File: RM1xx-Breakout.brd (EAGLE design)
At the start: 66.7 x 36.8 mm, 27 parts, among them IC3 MCP1703, J1 JUMPER_1X30805, J6 Lipo Battery

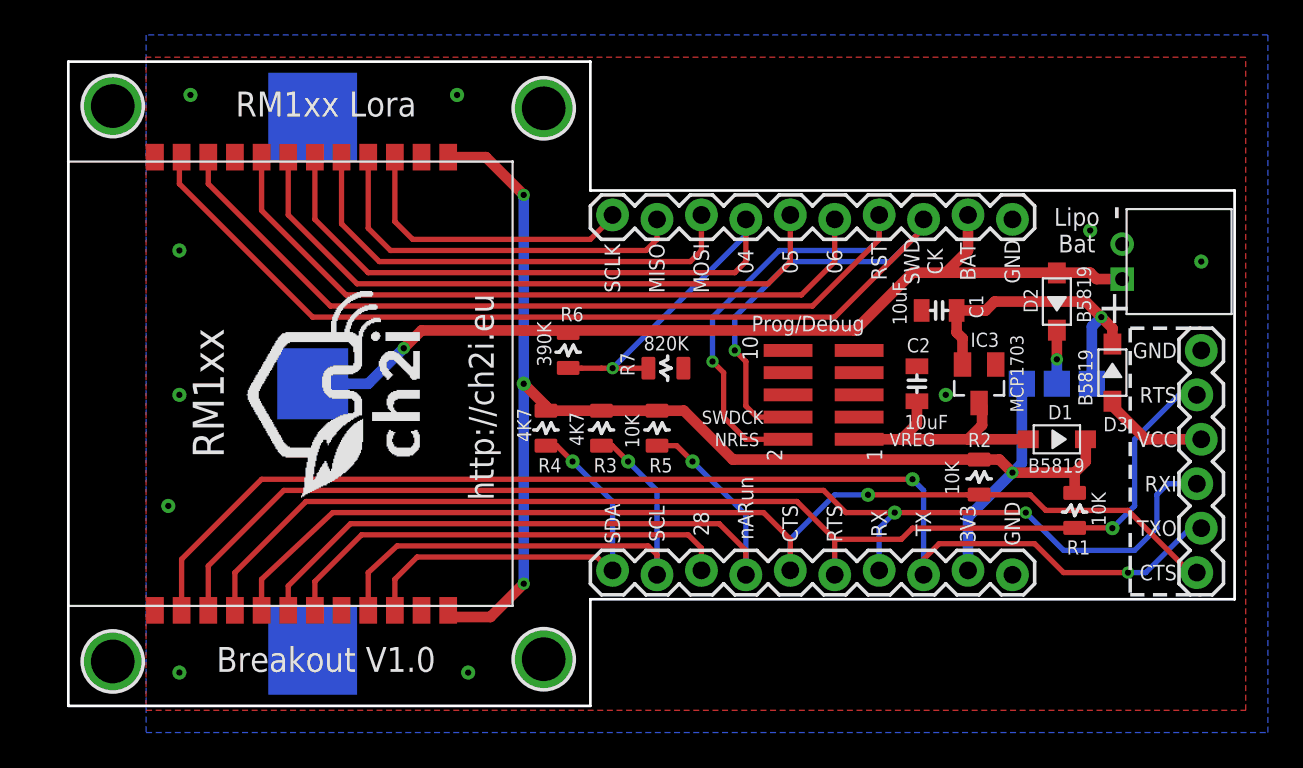
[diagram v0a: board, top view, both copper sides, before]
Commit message: removed copper on mounting holes
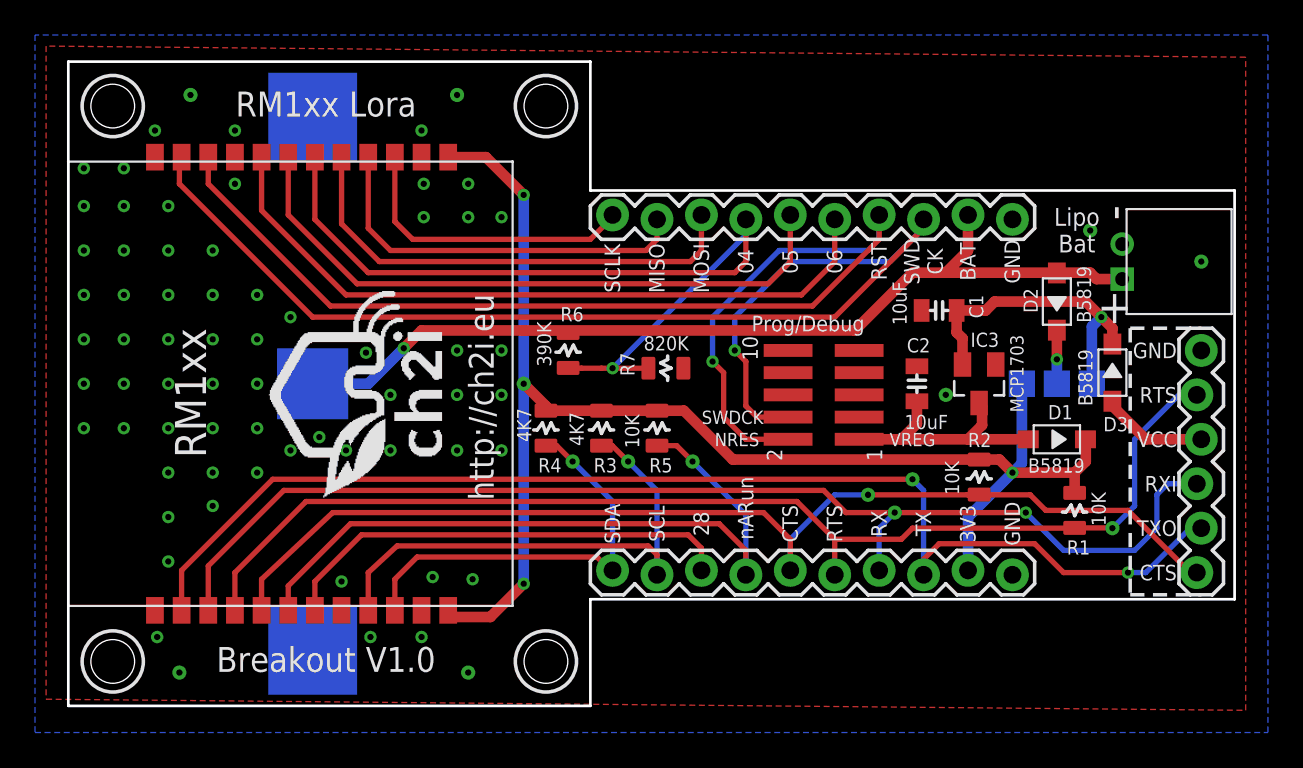
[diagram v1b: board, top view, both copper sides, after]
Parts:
- removed U$9: MOUNTINGHOLE2.5, microbuilder:MOUNTINGHOLE_2.5_PLATED
- added U$7: MOUNTINGHOLE2.5, microbuilder:MOUNTINGHOLE_2.5_PLATED
- moved U$8 31.7 mm to (13.3, 7.62)
- moved U$4 1.27 mm to (29.2, 23.5)
- moved U$6 0.18 mm to (38.1, 7.62)
- moved U$3 0.18 mm to (38.1, 39.4)

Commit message: version 1.0b
Removed copper from mounting holes
Added ground via under RM1xx module
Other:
- board text added: "Breakout V1.0a"
- board text added: "RM1xx Lora Breakoout V1.0a"
- board text removed: "Breakout V1.0"
- board text removed: "RM1xx Lora Breakoout V1.0"
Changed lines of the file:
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@@
 <text x="34.4043" y="22.733" size="1.4224" layer="21" font="vector" ratio="15" rot="R90" align="center">http://ch2i.eu</text>
 <text x="25.527" y="39.4843" size="1.4224" layer="21" font="vector" ratio="15" rot="R180" align="center">RM1xx Lora</text>
-<text x="25.527" y="7.7343" size="1.4224" layer="21" font="vector" ratio="15" rot="R180" align="center">Breakout V1.0</text>
+<text x="25.527" y="7.9883" size="1.4224" layer="21" font="vector" ratio="15" rot="R180" align="center">Breakout V1.0a</text>
 <text x="39.6367" y="22.987" size="1.3208" layer="22" font="vector" ratio="15" rot="MR90" align="center">RM1xx Lora
-Breakoout V1.0</text>
+Breakoout V1.0a</text>
 <text x="53.086" y="26.9367" size="0.889" layer="21" font="vector" ratio="15" align="center">Prog/Debug</text>
 <text x="56.8833" y="19.431" size="0.889" layer="21" font="vector" ratio="15" rot="R90" align="center">1</text>

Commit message: Version 1.1
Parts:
- added C3, C4, C5: 100nF, LowPowerLab:0805-CAP
- added P1: PADNORMAL, _c2h:PAD
- R6: value 390K -> 470K
- R7: value 820K -> 1M
- moved R1 0.32 mm to (68.3, 16.6)
- turned IC3 to 0 degrees
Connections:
- net 3V3: now also C3.1, C4.2
- net CTS: now also J2.2; no longer J2.6
- net GND: now also C3.2, C4.1, C5.1
- net NARUN: now also J2.6
- net RTS: now also P1.1; no longer J2.2
- net SIO04: now also C5.2
- net VIN: now also IC3.3; no longer IC3.2
- net VREG: now also IC3.2; no longer IC3.3
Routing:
- net NARUN: track 41.2 -> 74.5 mm, vias 1 -> 2
- net RTS: track 67.4 -> 59.7 mm
- net 3V3: track 81.7 -> 84.9 mm
- net RX: track 68.6 -> 65.7 mm
- net SIO04: track 48.4 -> 50.7 mm
- net CTS: track 64.5 -> 65.7 mm, vias 1 -> 2
- net TX: track 70.8 -> 69.7 mm
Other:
- board text added: "Breakout V1.1"
- board text added: "DTR"
- board text added: "RM1xx Lora Breakoout V1.1"
- board text removed: "Breakout V1.0a"
- board text removed: "RM1xx Lora Breakoout V1.0a"
